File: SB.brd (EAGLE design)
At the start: 78 x 34 mm, 47 parts, among them IC1 ATMEGA32U4NT-TQFP, IC2 HX711-SOP16L, J1 RJ10-WURTH, J2 AUDIO-JACK-PJ321, J3 USB-C-16P-16P, K1 HE721C-DIP, Q1 2N7002, Q2 2N3906, SW1 SWITCH-SPDT-4TABSSMT, SW2 SWITCH-SPDT-4TABSSMT, SW3 RESET, SW4 Trigger Level, SW5 Tare

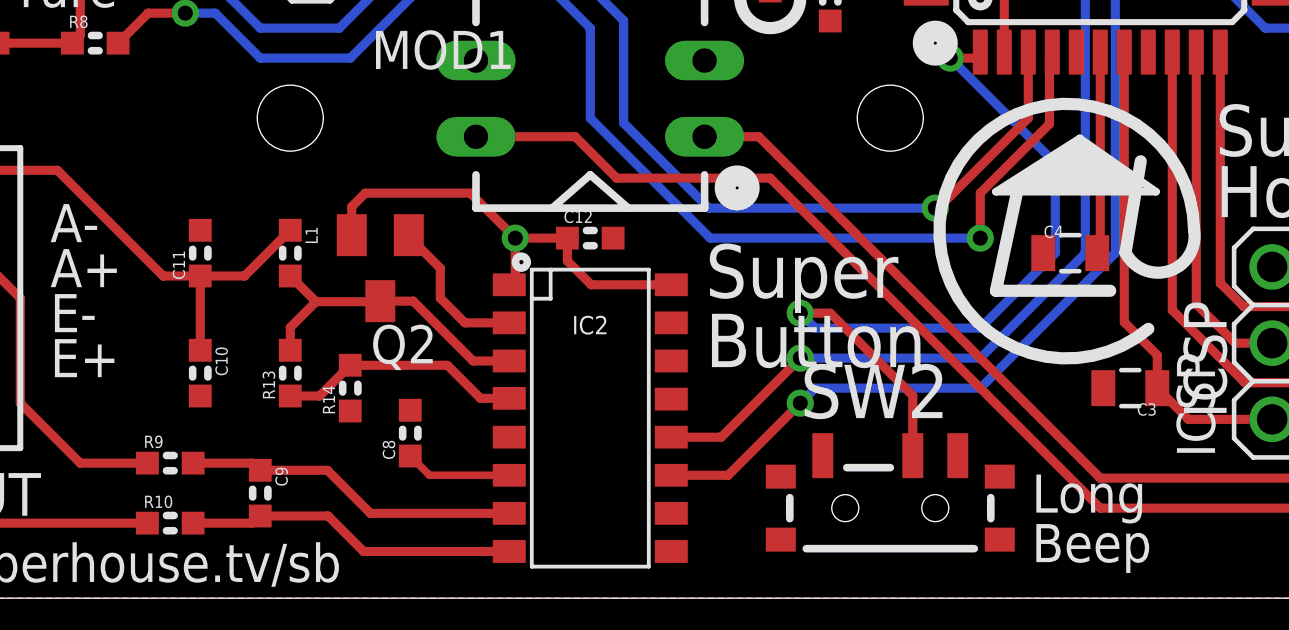
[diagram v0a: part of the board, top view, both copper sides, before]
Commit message: Replaced capacitors to simplify BOM for production
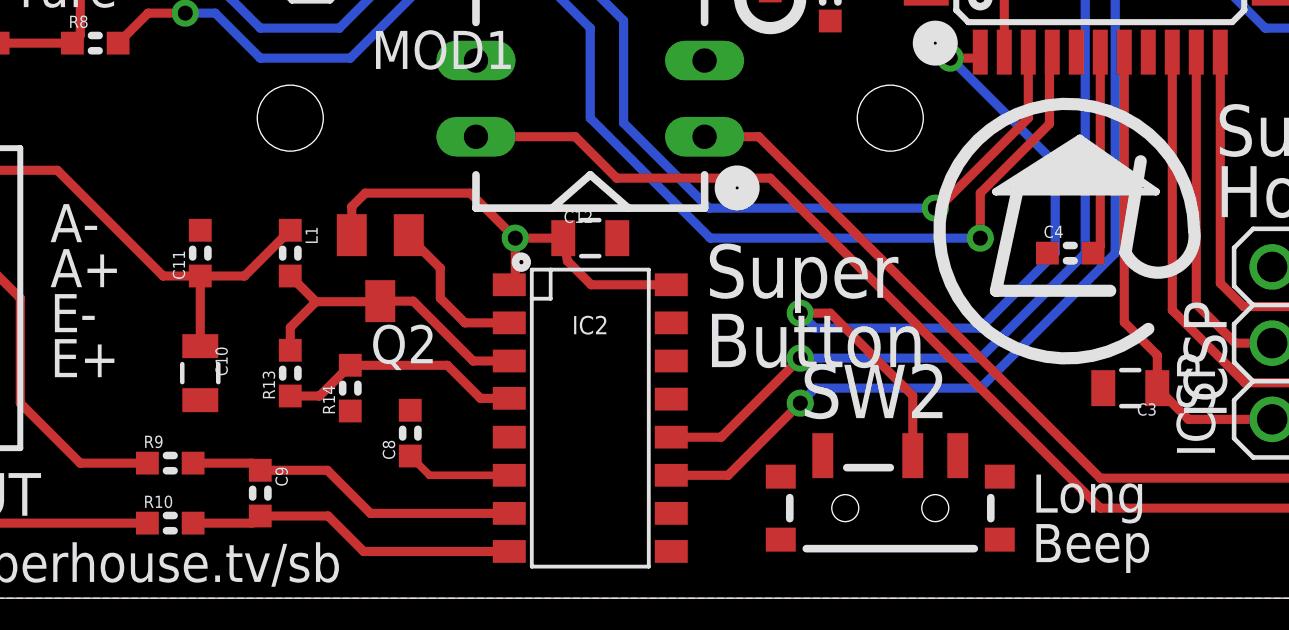
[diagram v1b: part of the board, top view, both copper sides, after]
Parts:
- C10, C12: device SuperHouse-DiscreteSemi:C0603 -> SuperHouse-DiscreteSemi:C0805
- C3: value 1uF -> 10uF
- C4: device SuperHouse-DiscreteSemi:C0805 -> SuperHouse-DiscreteSemi:C0603
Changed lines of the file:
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@@
 <?xml version="1.0" encoding="utf-8"?>
 <!DOCTYPE eagle SYSTEM "eagle.dtd">
-<eagle version="9.6.1">
+<eagle version="9.6.2">
 <drawing>
 <settings>
@@
 <setting verticaltext="up"/>
 </settings>
-<grid distance="0.5" unitdist="mm" unit="mm" style="lines" multiple="1" display="yes" altdistance="0.005" altunitdist="inch" altunit="inch"/>
+<grid distance="1" unitdist="mm" unit="mm" style="lines" multiple="1" display="yes" altdistance="0.005" altunitdist="inch" altunit="inch"/>
 <layers>
 <layer number="1" name="Top" color="12" fill="1" visible="yes" active="yes"/>
@@
 </layers>
 <board>
-<fusionsync huburn="a.cGVyc29uYWw6dWUyZDliZmNi" projecturn="a.cGVyc29uYWw6dWUyYmY2YTMwIzIwMTkxMjAzMjQ0MDMwNjUx" f3durn="urn:adsk.wipprod:dm.lineage:0njJKfu6R3STVv2jK1C-rg" pcbguid="d3339778-c5ae-47ed-addf-8a81f3fd190a" lastpulledtime="" lastsyncedchangeguid="658b777b-6f72-af3e-08d3-df1b217e5c50" latestrevisionid="" lastsyncedrevisionid="" lastboardhashguid="187c7758-43d3-ac97-906f-a3fd444c2922" lastpushedtime="2020-05-08T05:31:46Z" linktopcb3d="%12"/>
+<fusionsync huburn="a.cGVyc29uYWw6dWUyZDliZmNi" projecturn="a.cGVyc29uYWw6dWUyYmY2YTMwIzIwMTkxMjAzMjQ0MDMwNjUx" f3durn="urn:adsk.wipprod:dm.lineage:0njJKfu6R3STVv2jK1C-rg" pcbguid="d3339778-c5ae-47ed-addf-8a81f3fd190a" lastpulledtime="" lastsyncedchangeguid="658b777b-6f72-af3e-08d3-df1b217e5c50" latestrevisionid="" lastsyncedrevisionid="" lastboardhashguid="187c7758-43d3-ac97-906f-a3fd444c2922" lastpushedtime="2020-05-08T05:31:46Z" linktopcb3d="false"/>
 <plain>
 <wire x1="76" y1="34" x2="2" y2="34" width="0" layer="20"/>
@@
 <attribute name="VALUE" x="70.484" y="16.5348" size="0.8128" layer="27" font="vector"/>
 </element>
-<element name="C3" library="SuperHouse-DiscreteSemi" library_urn="urn:adsk.eagle:library:11768461" package="C0805" package3d_urn="urn:adsk.eagle:package:7066318/4" value="1uF" x="47" y="7" smashed="yes" rot="R180">
+<element name="C3" library="SuperHouse-DiscreteSemi" library_urn="urn:adsk.eagle:library:11768461" package="C0805" package3d_urn="urn:adsk.eagle:package:7066318/4" value="10uF" x="47" y="7" smashed="yes" rot="R180">
 <attribute name="NAME" x="47.889" y="6.492" size="0.4064" layer="25" font="vector" rot="R180"/>
 <attribute name="VALUE" x="45.484" y="7.5348" size="0.8128" layer="27" font="vector"/>
@@
 <attribute name="VALUE" x="55.984" y="29.0348" size="0.8128" layer="27" font="vector"/>
 </element>
-<element name="C4" library="SuperHouse-DiscreteSemi" library_urn="urn:adsk.eagle:library:11768461" package="C0805" package3d_urn="urn:adsk.eagle:package:7066318/4" value="1uF" x="45" y="11.5" smashed="yes">
+<element name="C4" library="SuperHouse-DiscreteSemi" library_urn="urn:adsk.eagle:library:11768461" package="C0603" package3d_urn="urn:adsk.eagle:package:7066315/6" value="1uF" x="45" y="11.5" smashed="yes">
 <attribute name="NAME" x="44.111" y="12.008" size="0.4064" layer="25" font="vector"/>
 <attribute name="VALUE" x="43.484" y="12.0348" size="0.8128" layer="27" font="vector"/>
@@
 <attribute name="VALUE" x="18.484" y="13.0348" size="0.8128" layer="27" font="vector"/>
 </element>
-<element name="C10" library="SuperHouse-DiscreteSemi" library_urn="urn:adsk.eagle:library:11768461" package="C0603" package3d_urn="urn:adsk.eagle:package:7066315/6" value="10uF" x="16" y="7.5" smashed="yes" rot="R270">
+<element name="C10" library="SuperHouse-DiscreteSemi" library_urn="urn:adsk.eagle:library:11768461" package="C0805" package3d_urn="urn:adsk.eagle:package:7066318/4" value="10uF" x="16" y="7.5" smashed="yes" rot="R270">
 <attribute name="NAME" x="16.508" y="8.389" size="0.4064" layer="25" font="vector" rot="R270"/>
 <attribute name="VALUE" x="14.484" y="9.0348" size="0.8128" layer="27" font="vector"/>
@@
 <attribute name="VALUE" x="14.984" y="13.0348" size="0.8128" layer="27" font="vector"/>
 </element>
-<element name="C12" library="SuperHouse-DiscreteSemi" library_urn="urn:adsk.eagle:library:11768461" package="C0603" package3d_urn="urn:adsk.eagle:package:7066315/6" value="10uF" x="29" y="12" smashed="yes">
+<element name="C12" library="SuperHouse-DiscreteSemi" library_urn="urn:adsk.eagle:library:11768461" package="C0805" package3d_urn="urn:adsk.eagle:package:7066318/4" value="10uF" x="29" y="12" smashed="yes">
 <attribute name="NAME" x="28.111" y="12.508" size="0.4064" layer="25" font="vector"/>
 <attribute name="VALUE" x="27.484" y="12.5348" size="0.8128" layer="27" font="vector"/>
@@
 <wire x1="75.5" y1="16" x2="72.262" y2="16" width="0.3048" layer="1"/>
 <wire x1="26.3" y1="10.445" x2="26.355" y2="10.5" width="0.254" layer="1"/>
-<wire x1="28.238" y1="11.238" x2="28.238" y2="12" width="0.3048" layer="1"/>
+<wire x1="28.238" y1="11.238" x2="28.1" y2="12" width="0.3048" layer="1"/>
 <wire x1="31.7" y1="10.445" x2="29.031" y2="10.445" width="0.3048" layer="1"/>
 <wire x1="29.031" y1="10.445" x2="28.238" y2="11.238" width="0.3048" layer="1"/>
 <via x="26.5" y="12" extent="1-16" drill="0.5"/>
-<wire x1="28.238" y1="12" x2="26.5" y2="12" width="0.3048" layer="1"/>
+<wire x1="28.1" y1="12" x2="26.5" y2="12" width="0.3048" layer="1"/>
 <wire x1="26.5" y1="12" x2="26.5" y2="10.645" width="0.3048" layer="1"/>
 <wire x1="26.5" y1="10.645" x2="26.3" y2="10.445" width="0.254" layer="1"/>
@@
 <contactref element="C4" pad="2"/>
 <contactref element="IC1" pad="6"/>
-<wire x1="46" y1="11.738" x2="45.9" y2="11.5" width="0.3048" layer="1"/>
+<wire x1="46" y1="11.738" x2="45.762" y2="11.5" width="0.3048" layer="1"/>
 <wire x1="46" y1="18.2" x2="46" y2="11.738" width="0.3048" layer="1"/>
 </signal>
@@
 <wire x1="19" y1="12.262" x2="17.476" y2="10.738" width="0.3048" layer="1"/>
 <wire x1="17.476" y1="10.738" x2="16" y2="10.738" width="0.3048" layer="1"/>
-<wire x1="16" y1="10.738" x2="16" y2="8.262" width="0.3048" layer="1"/>
+<wire x1="16" y1="10.738" x2="16" y2="8.4" width="0.3048" layer="1"/>
 <wire x1="11.238" y1="14.262" x2="7.022" y2="14.262" width="0.3048" layer="1"/>
 <wire x1="16" y1="10.738" x2="14.762" y2="10.738" width="0.3048" layer="1"/>
